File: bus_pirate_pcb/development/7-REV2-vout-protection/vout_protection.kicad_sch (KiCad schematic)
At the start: 21 parts, among them Q3 PMXB56EN, Q4 PMXB56EN, Q6 2N7002KT, U117 LM393BIDSGR

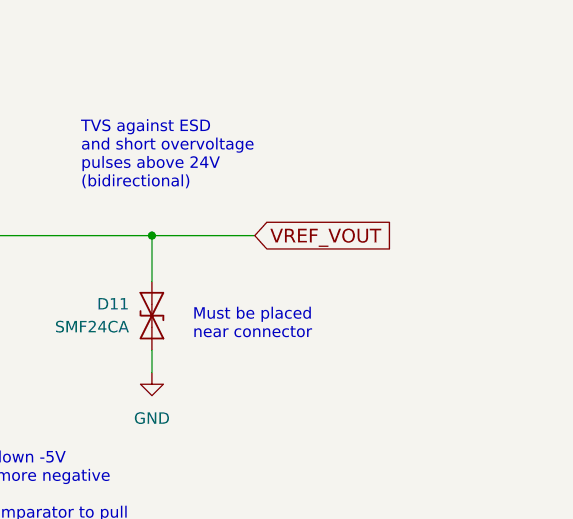
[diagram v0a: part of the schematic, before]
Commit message: BP 7R2 VOUT protection
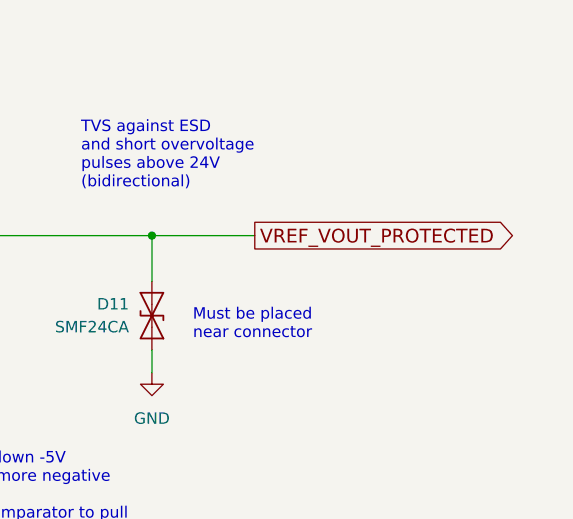
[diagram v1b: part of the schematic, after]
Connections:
- net VREF_VOUT: no longer D11.2 (A2), D18.1 (K), Q4.3 (D)
- new net VREF_VOUT_PROTECTED: D11.2 (A2), D18.1 (K), Q4.3 (D)

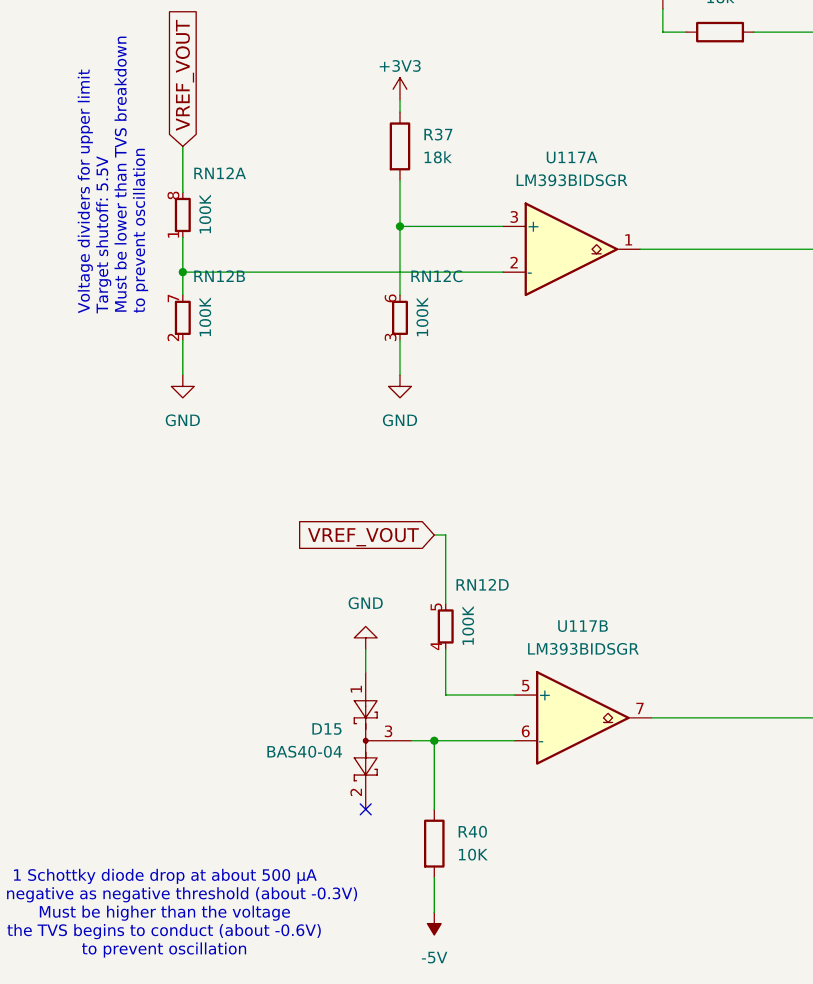
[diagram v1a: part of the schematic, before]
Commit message: 7R2 with vout protection
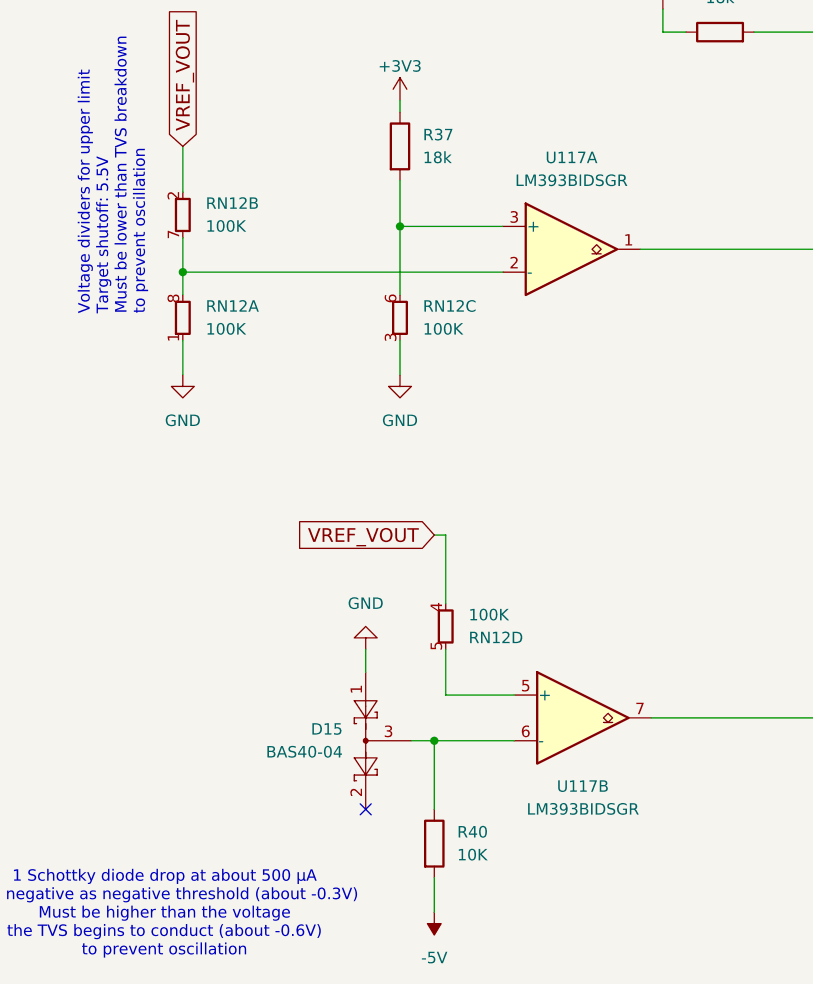
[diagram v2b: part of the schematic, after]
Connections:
- net GND: now also RN12.1 (R1.1); no longer RN12.2 (R1.1)
- net VREF_VOUT: now also RN12.2 (R1.1), RN12.4 (R1.1); no longer RN12.5 (R1.8), RN12.8 (R1.8)
- net at RN12.7 (R1.8), U117.2 (-): now also RN12.8 (R1.8); no longer RN12.1 (R1.1)
- net at U117.5 (+): now also RN12.5 (R1.8); no longer RN12.4 (R1.1)
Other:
- moved on the sheet: RN12A, RN12B, RN12D
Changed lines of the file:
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@@
 	(symbol
 		(lib_id "dp-rarray:R_Array")
-		(at 77.47 109.22 180)
+		(at 77.47 97.79 0)
+		(mirror y)
 		(unit 2)
 		(exclude_from_sim no)
@@
 		(on_board yes)
 		(dnp no)
+		(fields_autoplaced yes)
 		(property "Reference" "RN12"
-			(at 81.534 104.648 0)
+			(at 80.01 96.5199 0)
 			(effects
 				(font
 					(size 1.27 1.27)
 				)
+				(justify right)
 			)
 		)
 		(property "Value" "100K"
-			(at 80.01 109.22 90)
+			(at 80.01 99.0599 0)
 			(effects
 				(font
 					(size 1.27 1.27)
 				)
+				(justify right)
 			)
 		)
 		(property "Footprint" "Resistor_SMD:R_Array_Convex_4x0402"
-			(at 79.502 107.95 90)
+			(at 79.502 99.06 90)
 			(effects
 				(font
@@
 		)
 		(property "Datasheet" "http://www.vishay.com/docs/31509/csc.pdf"
-			(at 73.66 109.982 0)
+			(at 73.66 97.028 0)
 			(effects
 				(font
@@
 		)
 		(property "Description" ""
-			(at 77.47 109.22 0)
+			(at 77.47 97.79 0)
 			(effects
 				(font
@@
 		)
 		(property "RMB" "0.03666"
-			(at 77.47 109.22 0)
+			(at 77.47 97.79 0)
 			(effects
 				(font
@@
 		)
 		(property "Supplier" "https://item.szlcsc.com/635571.html"
-			(at 77.47 109.22 0)
+			(at 77.47 97.79 0)
 			(effects
 				(font
@@
 		)
 		(property "Description_1" ""
-			(at 77.47 109.22 0)
+			(at 77.47 97.79 0)
 			(effects
 				(font
@@
 		)
 		(property "MAXIMUM_PACKAGE_HEIGHT" ""
-			(at 77.47 109.22 0)
+			(at 77.47 97.79 0)
 			(effects
 				(font
@@
 		)
 		(property "PARTREV" ""
-			(at 77.47 109.22 0)
+			(at 77.47 97.79 0)
 			(effects
 				(font
@@
 		)
 		(property "STANDARD" ""
-			(at 77.47 109.22 0)
+			(at 77.47 97.79 0)
 			(effects
 				(font
@@
 	(symbol
 		(lib_id "dp-rarray:R_Array")
-		(at 106.68 143.51 180)
+		(at 106.68 143.51 0)
+		(mirror y)
 		(unit 4)
 		(exclude_from_sim no)
@@
 		(dnp no)
 		(property "Reference" "RN12"
-			(at 110.744 138.938 0)
+			(at 109.22 144.7801 0)
 			(effects
 				(font
 					(size 1.27 1.27)
 				)
+				(justify right)
 			)
 		)
 		(property "Value" "100K"
-			(at 109.22 143.51 90)
+			(at 109.22 142.2401 0)
 			(effects
 				(font
 					(size 1.27 1.27)
 				)
+				(justify right)
 			)
 		)
 		(property "Footprint" "Resistor_SMD:R_Array_Convex_4x0402"
-			(at 108.712 142.24 90)
+			(at 108.712 144.78 90)
 			(effects
 				(font
@@
 		)
 		(property "Datasheet" "http://www.vishay.com/docs/31509/csc.pdf"
-			(at 102.87 144.272 0)
+			(at 102.87 142.748 0)
 			(effects
 				(font
@@
 		(dnp no)
 		(property "Reference" "RN12"
-			(at 105.664 104.648 0)
+			(at 104.14 107.9499 0)
 			(effects
 				(font
 					(size 1.27 1.27)
 				)
+				(justify right)
 			)
 		)
 		(property "Value" "100K"
-			(at 104.14 109.22 90)
+			(at 104.14 110.4899 0)
 			(effects
 				(font
 					(size 1.27 1.27)
 				)
+				(justify right)
 			)
 		)
@@
 	(symbol
 		(lib_id "dp-rarray:R_Array")
-		(at 77.47 97.79 180)
+		(at 77.47 109.22 180)
 		(unit 1)
 		(exclude_from_sim no)
@@
 		(on_board yes)
 		(dnp no)
+		(fields_autoplaced yes)
 		(property "Reference" "RN12"
-			(at 81.534 93.218 0)
+			(at 80.01 107.9499 0)
 			(effects
 				(font
 					(size 1.27 1.27)
 				)
+				(justify right)
 			)
 		)
 		(property "Value" "100K"
-			(at 80.01 97.79 90)
+			(at 80.01 110.4899 0)
 			(effects
 				(font
 					(size 1.27 1.27)
 				)
+				(justify right)
 			)
 		)
 		(property "Footprint" "Resistor_SMD:R_Array_Convex_4x0402"
-			(at 79.502 96.52 90)
+			(at 79.502 107.95 90)
 			(effects
 				(font
@@
 		)
 		(property "Datasheet" "http://www.vishay.com/docs/31509/csc.pdf"
-			(at 73.66 98.552 0)
+			(at 73.66 109.982 0)
 			(effects
 				(font
@@
 		)
 		(property "Description" ""
-			(at 77.47 97.79 0)
+			(at 77.47 109.22 0)
 			(effects
 				(font
@@
 		)
 		(property "RMB" "0.03666"
-			(at 77.47 97.79 0)
+			(at 77.47 109.22 0)
 			(effects
 				(font
@@
 		)
 		(property "Supplier" "https://item.szlcsc.com/635571.html"
-			(at 77.47 97.79 0)
+			(at 77.47 109.22 0)
 			(effects
 				(font
@@
 		)
 		(property "Description_1" ""
-			(at 77.47 97.79 0)
+			(at 77.47 109.22 0)
 			(effects
 				(font
@@
 		)
 		(property "MAXIMUM_PACKAGE_HEIGHT" ""
-			(at 77.47 97.79 0)
+			(at 77.47 109.22 0)
 			(effects
 				(font
@@
 		)
 		(property "PARTREV" ""
-			(at 77.47 97.79 0)
+			(at 77.47 109.22 0)
 			(effects
 				(font
@@
 		)
 		(property "STANDARD" ""
-			(at 77.47 97.79 0)
+			(at 77.47 109.22 0)
 			(effects
 				(font
@@
 		(fields_autoplaced yes)
 		(property "Reference" "U117"
-			(at 121.92 143.51 0)
+			(at 121.92 161.29 0)
 			(effects
 				(font
@@
 		)
 		(property "Value" "LM393BIDSGR"
-			(at 121.92 146.05 0)
+			(at 121.92 163.83 0)
 			(effects
 				(font
